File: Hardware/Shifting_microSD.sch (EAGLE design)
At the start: 20 parts, among them J1 USD_CONNECTOR, U1 TXB0104, U2 3.3V

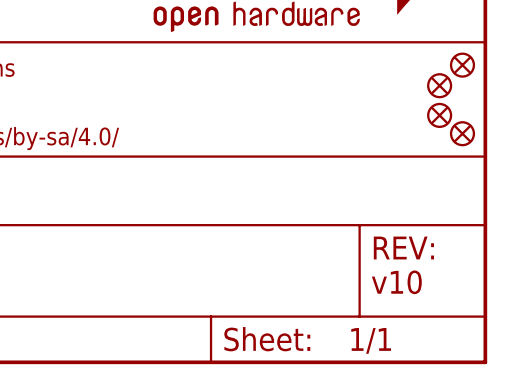
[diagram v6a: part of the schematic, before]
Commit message: Increased via sizes and shrunk PCB to exact width of header
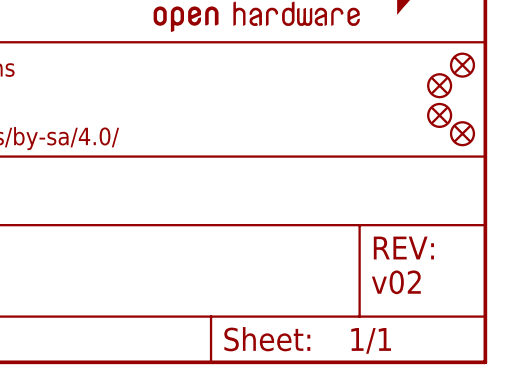
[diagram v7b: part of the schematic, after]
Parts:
- LOGO1: value SFE_LOGO_FLAME.3_INCH -> SFE_LOGO_FLAME.2_INCH; device SparkFun-Aesthetics:SFE_LOGO_FLAME.3_INCH -> SparkFun-Aesthetics:SFE_LOGO_FLAME.2_INCH
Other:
- note added: "v02"
- note removed: "v10"
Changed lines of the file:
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@@
 <grid distance="0.1" unitdist="inch" unit="inch" style="lines" multiple="1" display="no" altdistance="0.01" altunitdist="inch" altunit="inch"/>
 <layers>
-<layer number="1" name="Top" color="4" fill="1" visible="no" active="no"/>
-<layer number="2" name="Route2" color="1" fill="3" visible="no" active="no"/>
-<layer number="3" name="Route3" color="4" fill="3" visible="no" active="no"/>
-<layer number="4" name="Route4" color="1" fill="4" visible="no" active="no"/>
-<layer number="5" name="Route5" color="4" fill="4" visible="no" active="no"/>
-<layer number="6" name="Route6" color="1" fill="8" visible="no" active="no"/>
-<layer number="7" name="Route7" color="4" fill="8" visible="no" active="no"/>
-<layer number="8" name="Route8" color="1" fill="2" visible="no" active="no"/>
-<layer number="9" name="Route9" color="4" fill="2" visible="no" active="no"/>
-<layer number="10" name="Route10" color="1" fill="7" visible="no" active="no"/>
-<layer number="11" name="Route11" color="4" fill="7" visible="no" active="no"/>
-<layer number="12" name="Route12" color="1" fill="5" visible="no" active="no"/>
-<layer number="13" name="Route13" color="4" fill="5" visible="no" active="no"/>
-<layer number="14" name="Route14" color="1" fill="6" visible="no" active="no"/>
-<layer number="15" name="Route15" color="4" fill="6" visible="no" active="no"/>
-<layer number="16" name="Bottom" color="1" fill="1" visible="no" active="no"/>
-<layer number="17" name="Pads" color="2" fill="1" visible="no" active="no"/>
-<layer number="18" name="Vias" color="2" fill="1" visible="no" active="no"/>
-<layer number="19" name="Unrouted" color="6" fill="1" visible="no" active="no"/>
-<layer number="20" name="Dimension" color="15" fill="1" visible="no" active="no"/>
-<layer number="21" name="tPlace" color="16" fill="1" visible="no" active="no"/>
-<layer number="22" name="bPlace" color="14" fill="1" visible="no" active="no"/>
-<layer number="23" name="tOrigins" color="15" fill="1" visible="no" active="no"/>
-<layer number="24" name="bOrigins" color="15" fill="1" visible="no" active="no"/>
-<layer number="25" name="tNames" color="7" fill="1" visible="no" active="no"/>
-<layer number="26" name="bNames" color="7" fill="1" visible="no" active="no"/>
-<layer number="27" name="tValues" color="7" fill="1" visible="no" active="no"/>
-<layer number="28" name="bValues" color="7" fill="1" visible="no" active="no"/>
+<layer number="1" name="Top" color="4" fill="1" visible="yes" active="no"/>
+<layer number="2" name="Route2" color="1" fill="3" visible="yes" active="no"/>
+<layer number="3" name="Route3" color="4" fill="3" visible="yes" active="no"/>
+<layer number="4" name="Route4" color="1" fill="4" visible="yes" active="no"/>
+<layer number="5" name="Route5" color="4" fill="4" visible="yes" active="no"/>
+<layer number="6" name="Route6" color="1" fill="8" visible="yes" active="no"/>
+<layer number="7" name="Route7" color="4" fill="8" visible="yes" active="no"/>
+<layer number="8" name="Route8" color="1" fill="2" visible="yes" active="no"/>
+<layer number="9" name="Route9" color="4" fill="2" visible="yes" active="no"/>
+<layer number="10" name="Route10" color="1" fill="7" visible="yes" active="no"/>
+<layer number="11" name="Route11" color="4" fill="7" visible="yes" active="no"/>
+<layer number="12" name="Route12" color="1" fill="5" visible="yes" active="no"/>
+<layer number="13" name="Route13" color="4" fill="5" visible="yes" active="no"/>
+<layer number="14" name="Route14" color="1" fill="6" visible="yes" active="no"/>
+<layer number="15" name="Route15" color="4" fill="6" visible="yes" active="no"/>
+<layer number="16" name="Bottom" color="1" fill="1" visible="yes" active="no"/>
+<layer number="17" name="Pads" color="2" fill="1" visible="yes" active="no"/>
+<layer number="18" name="Vias" color="2" fill="1" visible="yes" active="no"/>
+<layer number="19" name="Unrouted" color="6" fill="1" visible="yes" active="no"/>
+<layer number="20" name="Dimension" color="6" fill="1" visible="yes" active="no"/>
+<layer number="21" name="tPlace" color="6" fill="1" visible="yes" active="no"/>
+<layer number="22" name="bPlace" color="6" fill="1" visible="yes" active="no"/>
+<layer number="23" name="tOrigins" color="15" fill="1" visible="yes" active="no"/>
+<layer number="24" name="bOrigins" color="15" fill="1" visible="yes" active="no"/>
+<layer number="25" name="tNames" color="7" fill="1" visible="yes" active="no"/>
+<layer number="26" name="bNames" color="7" fill="1" visible="yes" active="no"/>
+<layer number="27" name="tValues" color="7" fill="1" visible="yes" active="no"/>
+<layer number="28" name="bValues" color="7" fill="1" visible="yes" active="no"/>
 <layer number="29" name="tStop" color="7" fill="3" visible="no" active="no"/>
 <layer number="30" name="bStop" color="7" fill="6" visible="no" active="no"/>
@@
 <layer number="35" name="tGlue" color="7" fill="4" visible="no" active="no"/>
 <layer number="36" name="bGlue" color="7" fill="5" visible="no" active="no"/>
-<layer number="37" name="tTest" color="7" fill="1" visible="no" active="no"/>
-<layer number="38" name="bTest" color="7" fill="1" visible="no" active="no"/>
+<layer number="37" name="tTest" color="7" fill="1" visible="yes" active="no"/>
+<layer number="38" name="bTest" color="7" fill="1" visible="yes" active="no"/>
 <layer number="39" name="tKeepout" color="4" fill="11" visible="no" active="no"/>
 <layer number="40" name="bKeepout" color="1" fill="11" visible="no" active="no"/>
@@
 <layer number="44" name="Drills" color="7" fill="1" visible="no" active="no"/>
 <layer number="45" name="Holes" color="7" fill="1" visible="no" active="no"/>
-<layer number="46" name="Milling" color="3" fill="1" visible="no" active="no"/>
-<layer number="47" name="Measures" color="7" fill="1" visible="no" active="no"/>
-<layer number="48" name="Document" color="7" fill="1" visible="no" active="no"/>
-<layer number="49" name="Reference" color="3" fill="1" visible="no" active="no"/>
-<layer number="50" name="dxf" color="7" fill="1" visible="no" active="no"/>
-<layer number="51" name="tDocu" color="6" fill="1" visible="no" active="no"/>
-<layer number="52" name="bDocu" color="7" fill="1" visible="no" active="no"/>
-<layer number="53" name="tGND_GNDA" color="7" fill="9" visible="no" active="no"/>
-<layer number="54" name="bGND_GNDA" color="1" fill="9" visible="no" active="no"/>
-<layer number="56" name="wert" color="7" fill="1" visible="no" active="no"/>
-<layer number="57" name="tCAD" color="7" fill="1" visible="no" active="no"/>
-<layer number="59" name="tCarbon" color="7" fill="1" visible="no" active="no"/>
-<layer number="60" name="bCarbon" color="7" fill="1" visible="no" active="no"/>
+<layer number="46" name="Milling" color="3" fill="1" visible="yes" active="no"/>
+<layer number="47" name="Measures" color="7" fill="1" visible="yes" active="no"/>
+<layer number="48" name="Document" color="7" fill="1" visible="yes" active="no"/>
+<layer number="49" name="Reference" color="3" fill="1" visible="yes" active="no"/>
+<layer number="50" name="dxf" color="7" fill="1" visible="yes" active="no"/>
+<layer number="51" name="tDocu" color="6" fill="1" visible="yes" active="no"/>
+<layer number="52" name="bDocu" color="7" fill="1" visible="yes" active="no"/>
+<layer number="53" name="tGND_GNDA" color="7" fill="9" visible="yes" active="no"/>
+<layer number="54" name="bGND_GNDA" color="1" fill="9" visible="yes" active="no"/>
+<layer number="56" name="wert" color="7" fill="1" visible="yes" active="no"/>
+<layer number="57" name="tCAD" color="7" fill="1" visible="yes" active="no"/>
+<layer number="59" name="tCarbon" color="7" fill="1" visible="yes" active="no"/>
+<layer number="60" name="bCarbon" color="7" fill="1" visible="yes" active="no"/>
 <layer number="90" name="Modules" color="5" fill="1" visible="yes" active="yes"/>
 <layer number="91" name="Nets" color="2" fill="1" visible="yes" active="yes"/>
@@
 <part name="SUPPLY13" library="SparkFun-Aesthetics" deviceset="VCC" device=""/>
 <part name="GND1" library="SparkFun-Aesthetics" deviceset="GND" device=""/>
-<part name="LOGO1" library="SparkFun-Aesthetics" deviceset="SFE_LOGO_FLAME" device=".3_INCH"/>
+<part name="LOGO1" library="SparkFun-Aesthetics" deviceset="SFE_LOGO_FLAME" device=".2_INCH" value="SFE_LOGO_FLAME.2_INCH"/>
 <part name="LOGO2" library="SparkFun-Aesthetics" deviceset="OSHW-LOGO" device="S"/>
 <part name="U1" library="SparkFun-DigitalIC" deviceset="TXB0104PWR" device="SOIC14" value="TXB0104"/>
@@
 <plain>
 <text x="166.116" y="11.43" size="2.54" layer="94">Brent Wilkins</text>
-<text x="236.22" y="7.62" size="2.54" layer="94" font="vector">v10</text>
+<text x="236.22" y="7.62" size="2.54" layer="94" font="vector">v02</text>
 <text x="121.92" y="172.72" size="1.778" layer="97" font="vector" ratio="15" align="center">VCC +3.3V to +5.0V
 EXPECT UP TO VCC ON SIGNAL LINES</text>

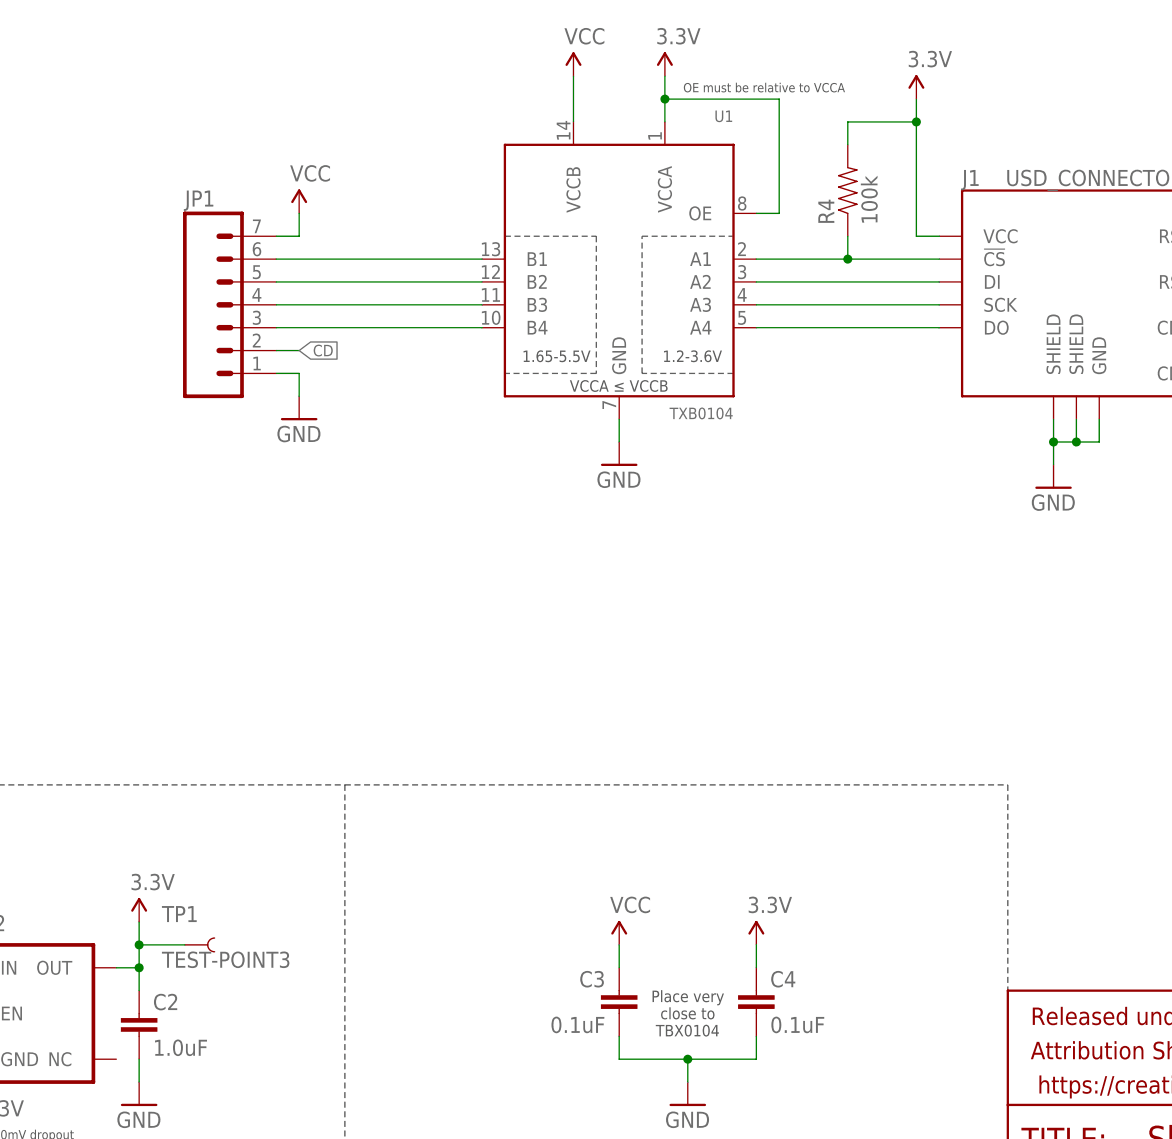
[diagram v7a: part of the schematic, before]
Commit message: Renamed a jack to JP and moved over a test point
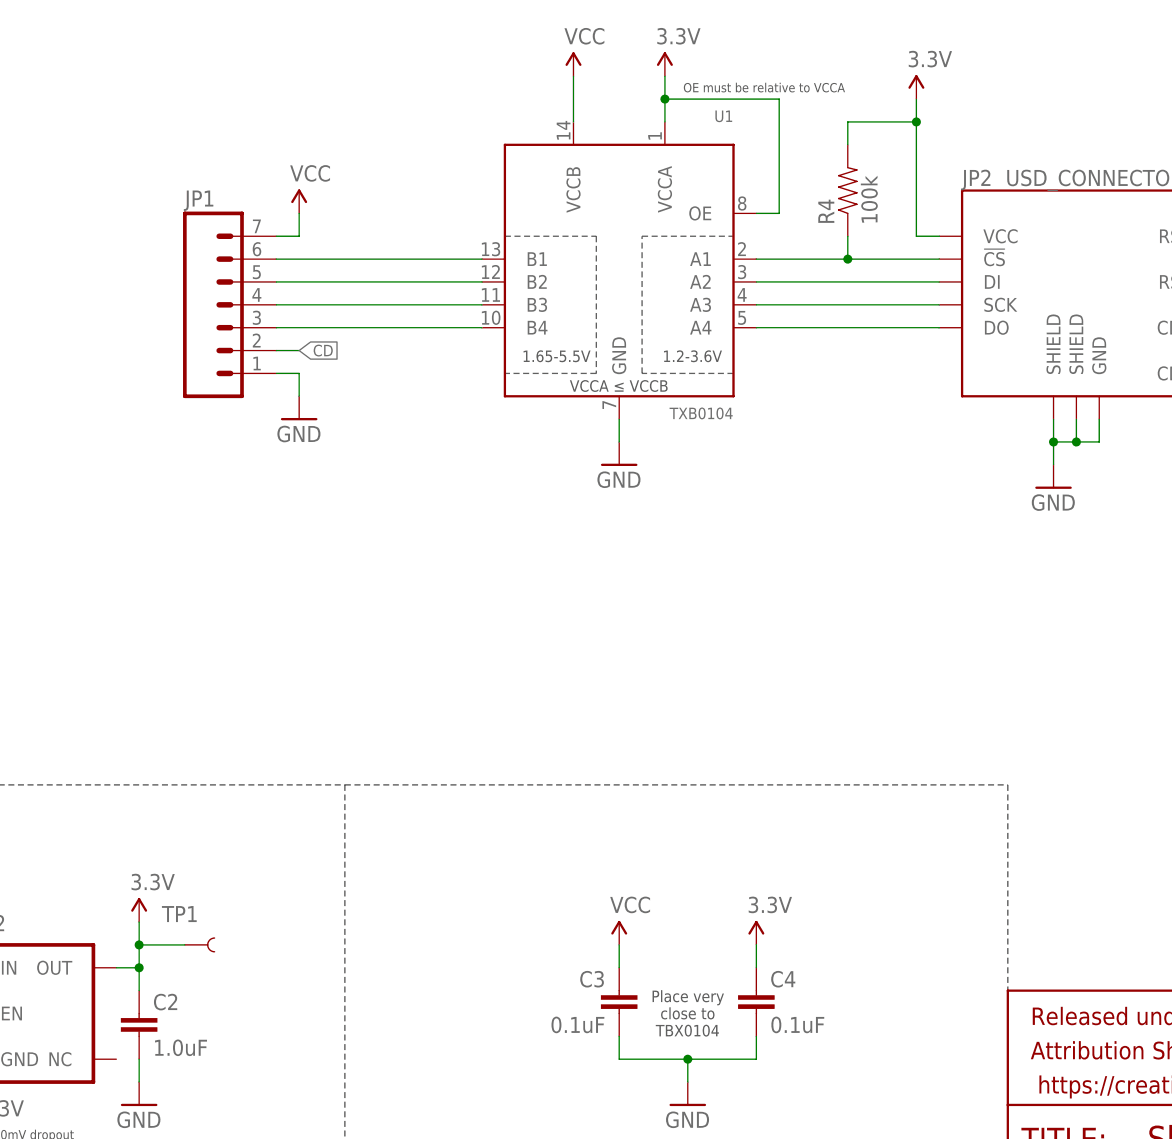
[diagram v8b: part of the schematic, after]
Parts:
- renumbered J1 to JP2
